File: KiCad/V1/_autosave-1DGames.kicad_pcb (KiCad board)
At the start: 2 copper layers, 100 x 70 mm, 10 parts, among them Q1 AO3401A, Q2 AO3401A, U1 ESP32-DEVKITC-32D

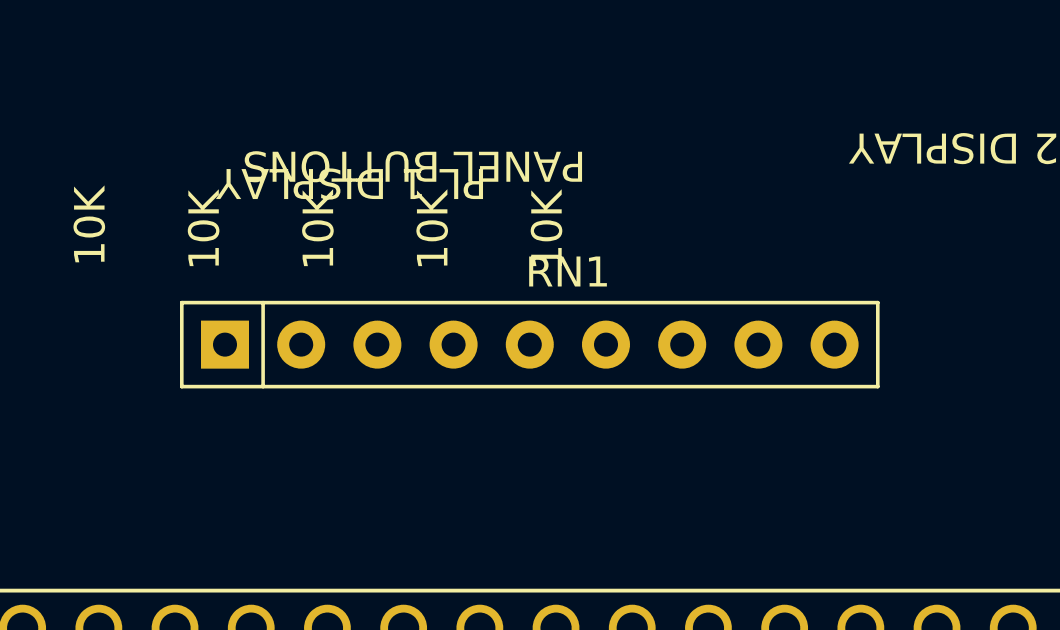
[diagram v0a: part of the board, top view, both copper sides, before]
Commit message: Worms joystick working, next: show joystick status in UI (including button).
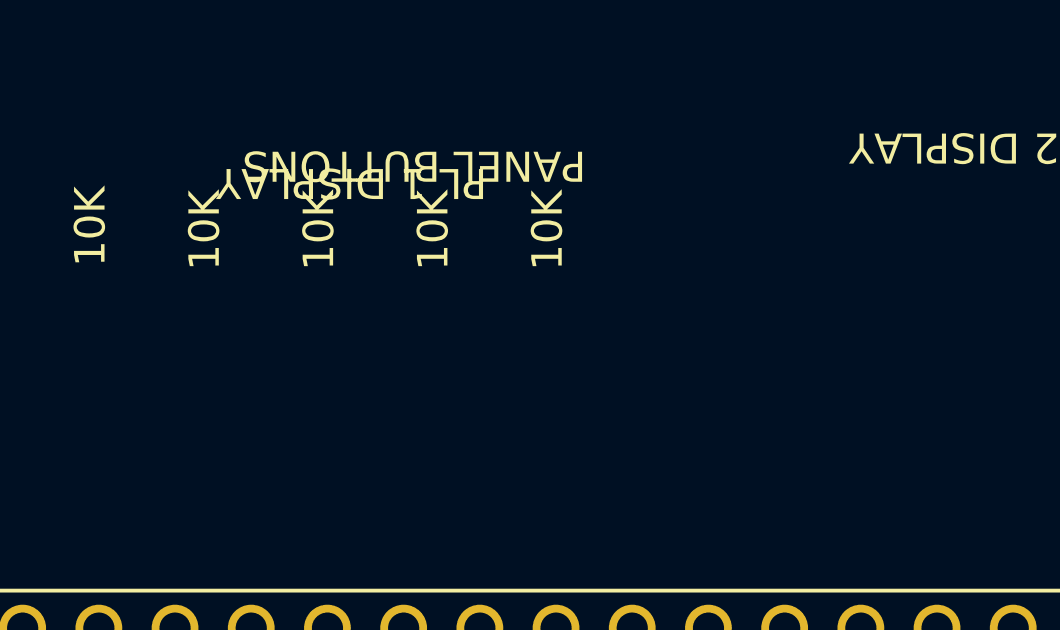
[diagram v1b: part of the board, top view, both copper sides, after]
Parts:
- removed RN1: 10K, Resistor_THT:R_Array_SIP9
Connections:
- net /P1_DISP_CLK renamed /LED_SEGMENTS_CLK
- net /P1_DISP_DIN renamed /LED_SEGMENTS_DIN
- U1 pad 27: /BUTTONS_PARALLEL_LOAD_INPUT -> unconnected-(U1-Pad27)
- U1 pad 28: /BUTTONS_CLOCK_INPUT -> unconnected-(U1-Pad28)
- U1 pad 29: /BUTTONS_SERIAL_OUTPUT -> unconnected-(U1-Pad29)

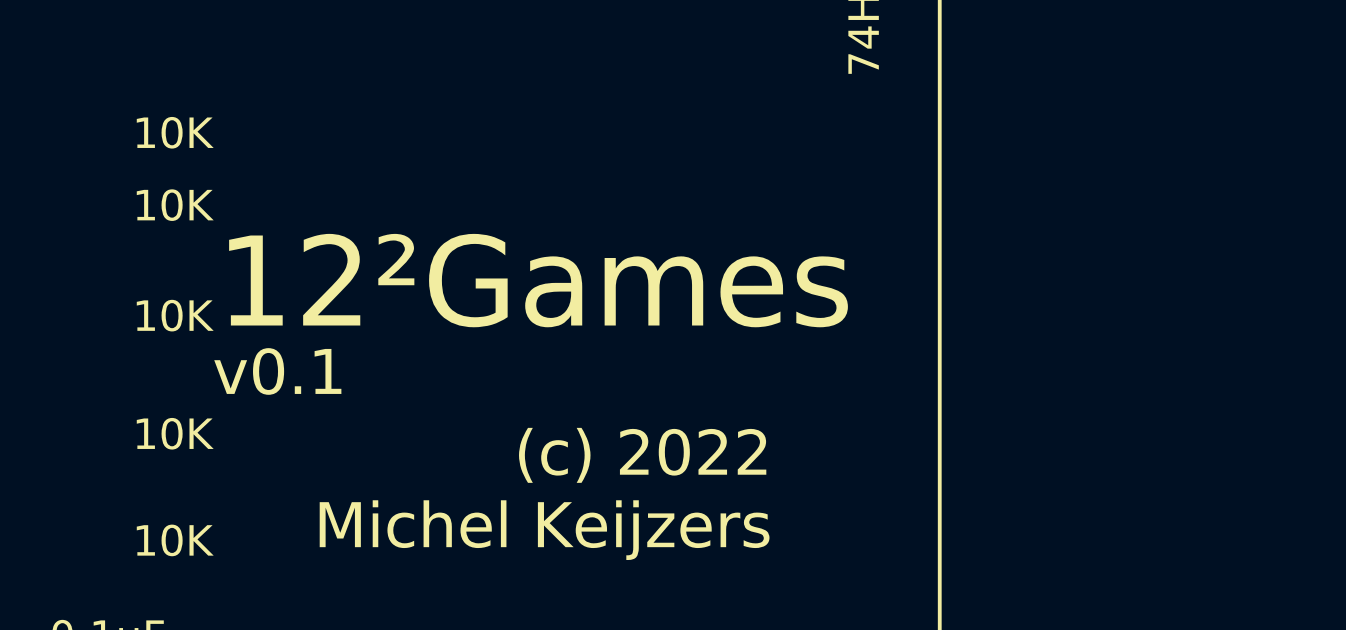
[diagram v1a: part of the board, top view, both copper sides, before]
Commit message: Compilable for Arduino Uno
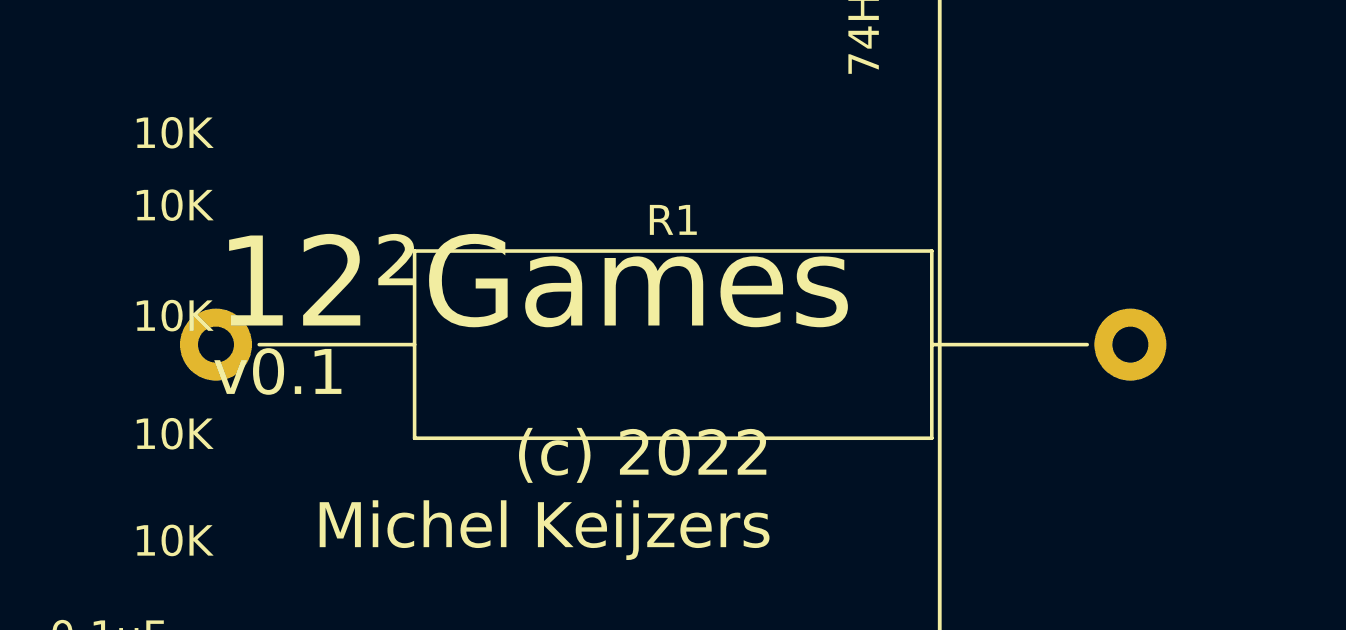
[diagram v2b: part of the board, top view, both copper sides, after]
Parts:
- added R1: 1K, Resistor_THT:R_Axial_DIN0617_L17.0mm_D6.0mm_P30.48mm_Horizontal, F.Cu at (42.7, 64.2)
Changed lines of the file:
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@@
   (net 37 "unconnected-(U1-Pad28)")
   (net 38 "unconnected-(U1-Pad29)")
+  (net 39 "Net-(R1-Pad2)")
   (footprint "MountingHole:MountingHole_3.2mm_M3" (layer "F.Cu")
     (at 119 45)
@@
       ) (layer "F.SilkS") (width 0.01) (fill solid))
   )
+  (footprint "Resistor_THT:R_Axial_DIN0617_L17.0mm_D6.0mm_P30.48mm_Horizontal" (layer "F.Cu")
+    (at 42.725 64.175)
+    (descr "Resistor, Axial_DIN0617 series, Axial, Horizontal, pin pitch=30.48mm, 2W, length*diameter=17*6mm^2, http://www.vishay.com/docs/20128/wkxwrx.pdf")
+    (tags "Resistor Axial_DIN0617 series Axial Horizontal pin pitch 30.48mm 2W length 17mm diameter 6mm")
+    (property "Sheetfile" "1DGames.kicad_sch")
+    (property "Sheetname" "")
+    (attr through_hole)
+    (fp_text reference "R1" (at 15.24 -4.12) (layer "F.SilkS")
+      (effects (font (size 1 1) (thickness 0.15)))
+    )
+    (fp_text value "1K" (at 15.24 4.12) (layer "F.Fab")
+      (effects (font (size 1 1) (thickness 0.15)))
+    )
+    (fp_text user "${REFERENCE}" (at 15.24 0) (layer "F.Fab")
+      (effects (font (size 1 1) (thickness 0.15)))
+    )
+    (fp_line (start 6.62 3.12) (end 23.86 3.12) (layer "F.SilkS") (width 0.12))
+    (fp_line (start 29.04 0) (end 23.86 0) (layer "F.SilkS") (width 0.12))
+    (fp_line (start 1.44 0) (end 6.62 0) (layer "F.SilkS") (width 0.12))
+    (fp_line (start 6.62 -3.12) (end 6.62 3.12) (layer "F.SilkS") (width 0.12))
+    (fp_line (start 23.86 -3.12) (end 6.62 -3.12) (layer "F.SilkS") (width 0.12))
+    (fp_line (start 23.86 3.12) (end 23.86 -3.12) (layer "F.SilkS") (width 0.12))
+    (fp_line (start 31.94 3.25) (end 31.94 -3.25) (layer "F.CrtYd") (width 0.05))
+    (fp_line (start -1.45 -3.25) (end -1.45 3.25) (layer "F.CrtYd") (width 0.05))
+    (fp_line (start -1.45 3.25) (end 31.94 3.25) (layer "F.CrtYd") (width 0.05))
+    (fp_line (start 31.94 -3.25) (end -1.45 -3.25) (layer "F.CrtYd") (width 0.05))
+    (fp_line (start 30.48 0) (end 23.74 0) (layer "F.Fab") (width 0.1))
+    (fp_line (start 0 0) (end 6.74 0) (layer "F.Fab") (width 0.1))
+    (fp_line (start 23.74 -3) (end 6.74 -3) (layer "F.Fab") (width 0.1))
+    (fp_line (start 6.74 -3) (end 6.74 3) (layer "F.Fab") (width 0.1))
+    (fp_line (start 23.74 3) (end 23.74 -3) (layer "F.Fab") (width 0.1))
+    (fp_line (start 6.74 3) (end 23.74 3) (layer "F.Fab") (width 0.1))
+    (pad "1" thru_hole circle locked (at 0 0) (size 2.4 2.4) (drill 1.2) (layers *.Cu *.Mask)
+      (net 19 "/SPEAKER_DRAIN") (pintype "passive"))
+    (pad "2" thru_hole oval locked (at 30.48 0) (size 2.4 2.4) (drill 1.2) (layers *.Cu *.Mask)
+      (net 39 "Net-(R1-Pad2)") (pintype "passive"))
+    (model "${KICAD6_3DMODEL_DIR}/Resistor_THT.3dshapes/R_Axial_DIN0617_L17.0mm_D6.0mm_P30.48mm_Horizontal.wrl"
+      (offset (xyz 0 0 0))
+      (scale (xyz 1 1 1))
+      (rotate (xyz 0 0 0))
+    )
+  )
   (footprint "ESP32:MODULE_ESP32-DEVKITC-32D" (layer "F.Cu")
